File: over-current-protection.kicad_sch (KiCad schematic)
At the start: 14 parts, among them U7 TL331, U8 INA169, U9 TLV9001IDCK

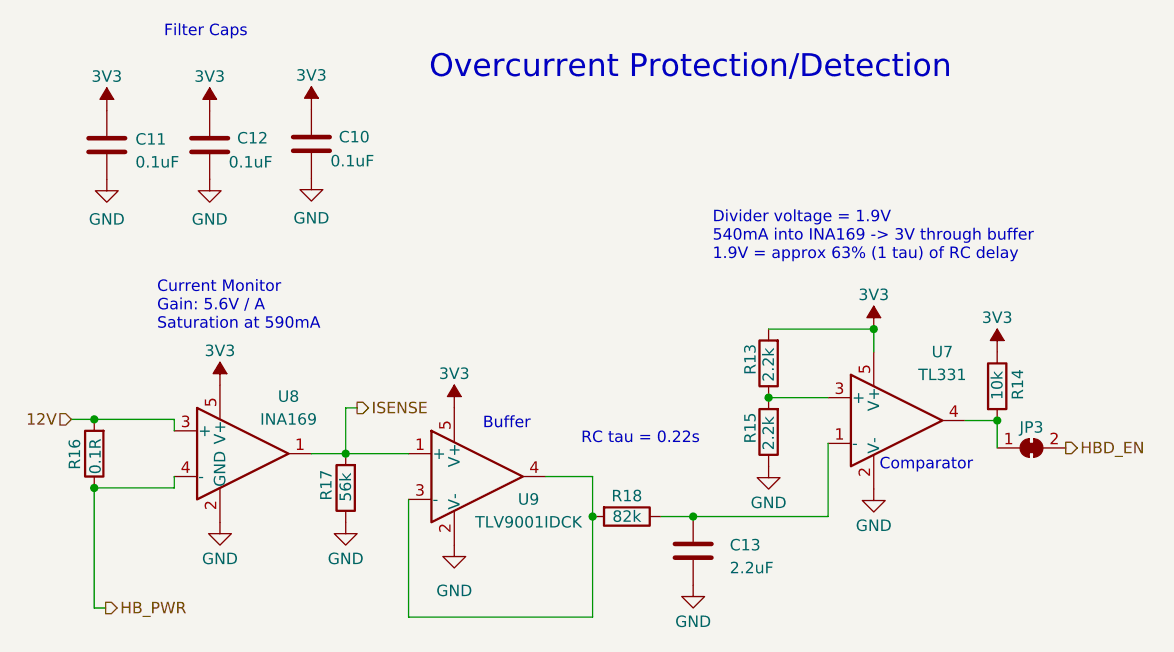
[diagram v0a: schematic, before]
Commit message: schematic draft 2; no FPC connections, no testpoints
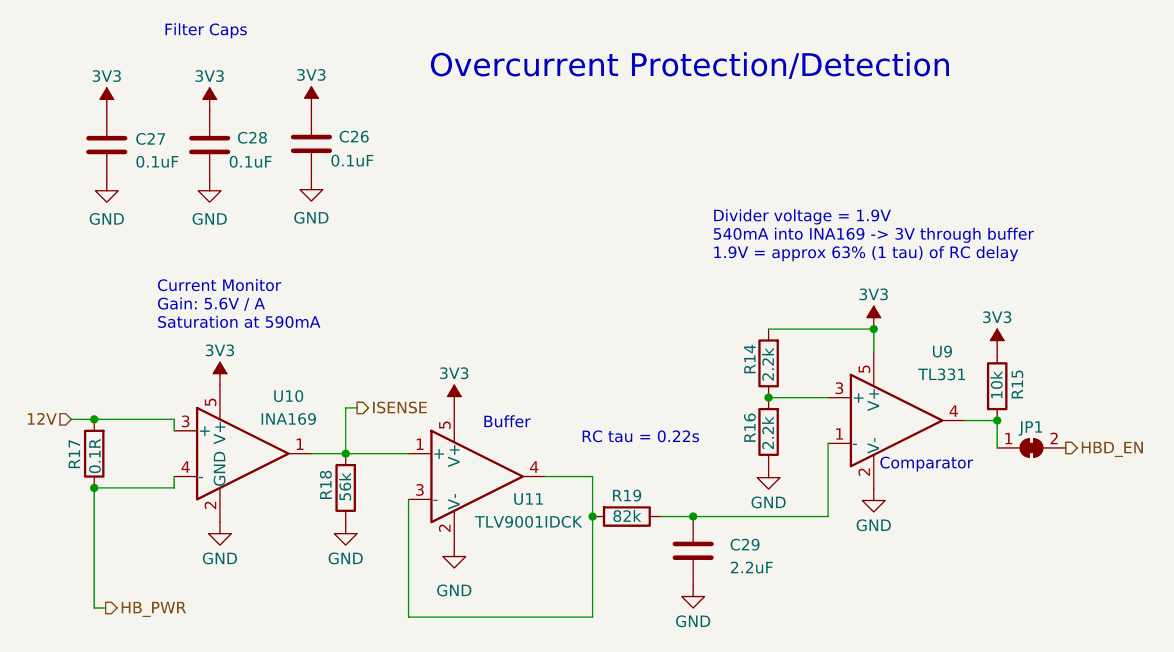
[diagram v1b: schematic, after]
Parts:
- renumbered C10 to C26, C11 to C27, C12 to C28, C13 to C29, JP3 to JP1, R13 to R14, R14 to R15, R15 to R16, R16 to R17, R17 to R18, R18 to R19, U8 to U10, U9 to U11, U7 to U9

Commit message: layout start
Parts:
- removed JP1: SolderJumper_2_Bridged, Jumper:SolderJumper-2_P1.3mm_Bridged_RoundedPad1.0x1.5mm, symbol Jumper:SolderJumper_2_Bridged
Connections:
- net HBD_EN: now also R15.2, U9.4
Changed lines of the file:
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@@
+	(wire
+		(pts
+			(xy 195.58 103.505) (xy 203.2 103.505)
+		)
+		(stroke
+			(width 0)
+			(type default)
+		)
+	)
 	(wire
 		(pts
@@
 					(unit 1)
 				)
-			)
-		)
-	)
-	(symbol
-		(lib_id "Jumper:SolderJumper_2_Bridged")
-		(at 199.39 103.505 0)
-		(unit 1)
-		(exclude_from_sim no)
-		(in_bom no)
-		(on_board yes)
-		(dnp no)
-		(property "Reference" "JP1"
-			(at 199.39 101.219 0)
-			(effects
-				(font
-					(size 1.27 1.27)
-				)
-			)
-		)
-		(property "Value" "SolderJumper_2_Bridged"
-			(at 199.39 101.219 0)
-			(effects
-				(font
-					(size 1.27 1.27)
-				)
-				(hide yes)
-			)
-		)
-		(property "Footprint" "Jumper:SolderJumper-2_P1.3mm_Bridged_RoundedPad1.0x1.5mm"
-			(at 199.39 103.505 0)
-			(effects
-				(font
-					(size 1.27 1.27)
-				)
-				(hide yes)
-			)
-		)
-		(property "Datasheet" "~"
-			(at 199.39 103.505 0)
-			(effects
-				(font
-					(size 1.27 1.27)
-				)
-				(hide yes)
-			)
-		)
-		(property "Description" ""
-			(at 199.39 103.505 0)
-			(effects
-				(font
-					(size 1.27 1.27)
-				)
-				(hide yes)
-			)
-		)
-		(pin "1"
-		)
-		(pin "2"
-		)
-		(instances
-			(project "nrf52-controller"
-				(path "/8f322677-487e-4d64-8621-277f6fdcdbee/aec39160-a535-4f8f-8def-dfb7034fab6e"
-					(reference "JP1")
-					(unit 1)
-				)
